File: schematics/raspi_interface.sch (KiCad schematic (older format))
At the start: 8 parts, among them P2 CONN_01X07, P3 CONN_02X20, U1 PS2502-1-A, U2 PS2502-1-A, U3 PS2502-1-A

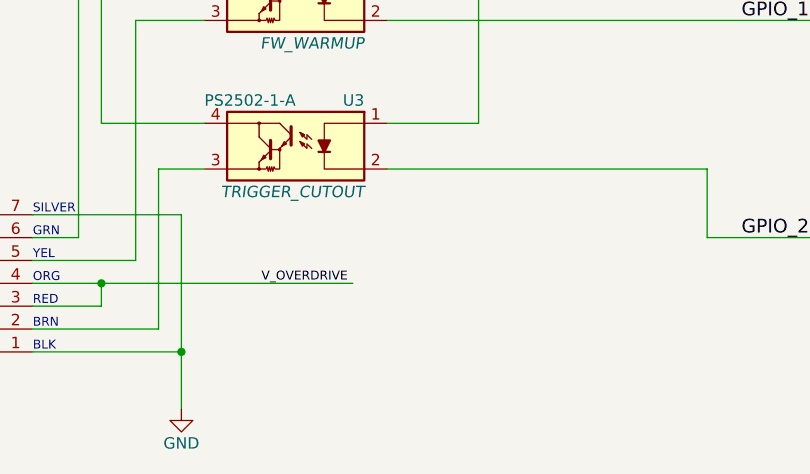
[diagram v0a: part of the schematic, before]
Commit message: Added D10, Schottky diode, to prevent backfeeding into power control board from gun batteries
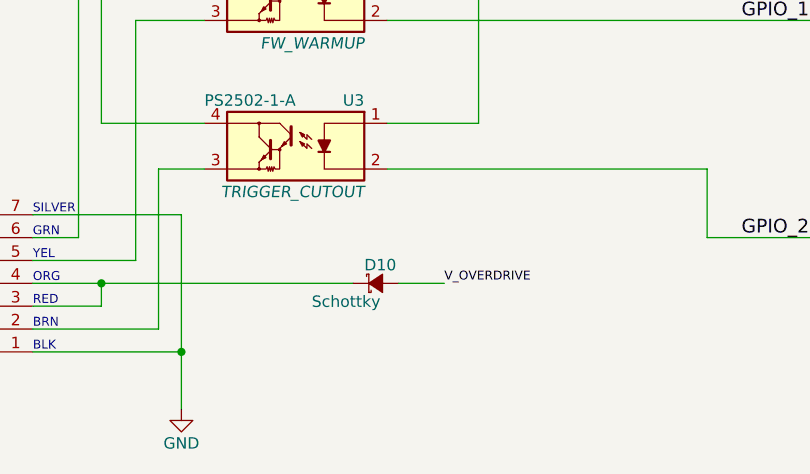
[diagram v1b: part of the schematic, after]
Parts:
- added D10: Schottky, symbol D_Schottky_Small
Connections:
- wire segments 58 -> 59
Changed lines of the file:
@@
 	2950 5050 2950 4950
 Connection ~ 2950 4950
-Text Label 3650 4950 0    39   ~ 0
+Text Label 4450 4950 0    39   ~ 0
 V_OVERDRIVE
 Text HLabel 1150 1500 0    60   Input ~ 0
@@
 Text Label 1950 1600 0    60   ~ 0
 GPIO_6
+$Comp
+L D_Schottky_Small D10
+U 1 1 58DE76F4
+P 4150 4950
+F 0 "D10" H 4100 5030 50  0000 L CNN
+F 1 "Schottky" H 3870 4870 50  0000 L CNN
+F 2 "" V 4150 4950 50  0000 C CNN
+F 3 "" V 4150 4950 50  0000 C CNN
+	1    4150 4950
+	1    0    0    -1
+$EndComp
+Wire Wire Line
+	4250 4950 4450 4950
 $EndSCHEMATC
